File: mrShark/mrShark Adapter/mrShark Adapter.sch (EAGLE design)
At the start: 23 parts, among them CON1 DF12-20DS, IC1 LM317MBSTT3, IC2 MCP73832T-2DCI/OT, IC3 MCP73832T-2DCI/OT, IC4 FT232RQ

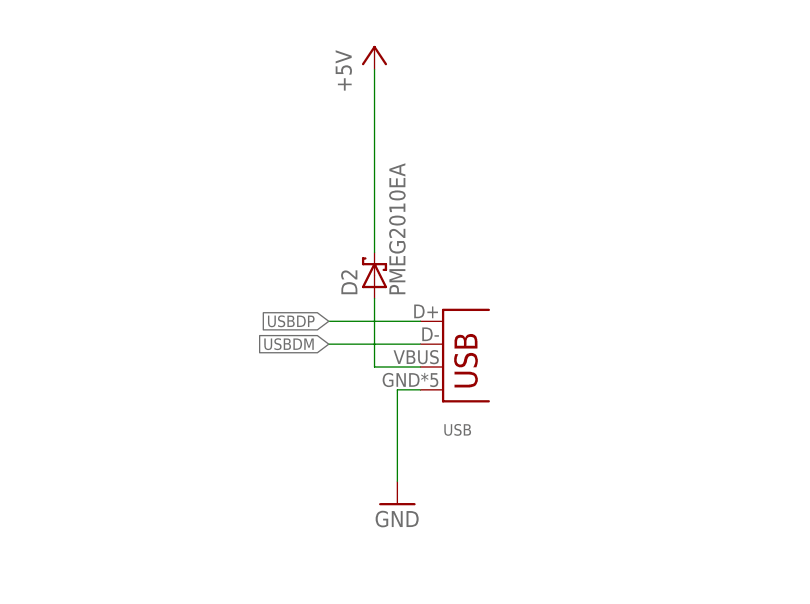
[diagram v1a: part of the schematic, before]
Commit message: Updated adapter to hirose mini usb connector
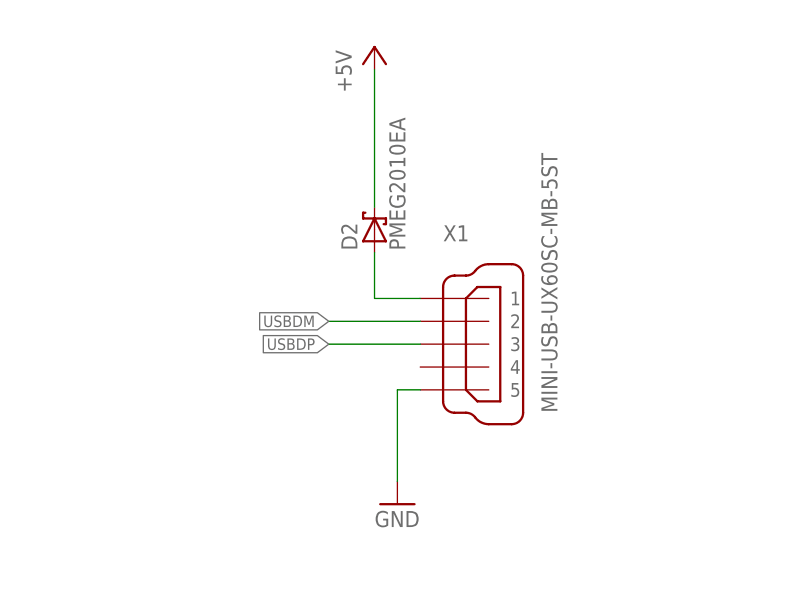
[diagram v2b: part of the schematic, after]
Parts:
- removed USB: (no value), con-usb-3:USB-MIC-S
- added X1: MINI-USB-UX60SC-MB-5ST, con-hirose:MINI-USB-UX60SC-MB-5ST
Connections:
- net GND: now also X1.5; no longer USB.GND
- net N$9: now also X1.1; no longer USB.VBUS
- net USBDM: now also X1.2; no longer USB.D-
- net USBDP: now also X1.3; no longer USB.D+
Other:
- moved on the sheet: D2
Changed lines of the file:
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@@
 <attribute name="TP_SIGNAL_NAME" value=""/>
 </part>
-<part name="USB" library="con-usb-3" deviceset="USB" device="-MIC-S"/>
 <part name="GND12" library="supply1" deviceset="GND" device=""/>
 <part name="D1" library="diode" deviceset="PMEG2010EA" device="R" value="PMEG2010EA"/>
@@
 <part name="P+4" library="supply1" deviceset="+5V" device=""/>
 <part name="P+10" library="supply1" deviceset="+5V" device=""/>
+<part name="X1" library="con-hirose" deviceset="MINI-USB-" device="UX60SC-MB-5ST"/>
 </parts>
 <sheets>
@@
 <instance part="TP4" gate="G$1" x="121.92" y="30.48"/>
 <instance part="TP5" gate="G$1" x="129.54" y="30.48"/>
-<instance part="USB" gate="G$1" x="127" y="129.54"/>
 <instance part="GND12" gate="1" x="121.92" y="116.84"/>
 <instance part="D1" gate="G$1" x="134.62" y="86.36" rot="R90"/>
-<instance part="D2" gate="G$1" x="119.38" y="142.24" rot="R90"/>
+<instance part="D2" gate="G$1" x="119.38" y="147.32" rot="R90"/>
 <instance part="ISP" gate="A" x="119.38" y="73.66"/>
 <instance part="P+4" gate="1" x="119.38" y="167.64"/>
 <instance part="P+10" gate="1" x="134.62" y="104.14"/>
+<instance part="X1" gate="G$1" x="129.54" y="134.62"/>
 </instances>
 <busses>
@@
 </segment>
 <segment>
-<pinref part="USB" gate="G$1" pin="GND"/>
 <pinref part="GND12" gate="1" pin="GND"/>
 <wire x1="124.46" y1="129.54" x2="121.92" y2="129.54" width="0.1524" layer="91"/>
 <wire x1="121.92" y1="129.54" x2="121.92" y2="119.38" width="0.1524" layer="91"/>
+<pinref part="X1" gate="G$1" pin="5"/>
 </segment>
 <segment>
@@
 <pinref part="D2" gate="G$1" pin="C"/>
 <pinref part="P+4" gate="1" pin="+5V"/>
-<wire x1="119.38" y1="144.78" x2="119.38" y2="165.1" width="0.1524" layer="91"/>
+<wire x1="119.38" y1="149.86" x2="119.38" y2="165.1" width="0.1524" layer="91"/>
 </segment>
 <segment>
@@
 </segment>
 <segment>
-<pinref part="USB" gate="G$1" pin="D+"/>
-<wire x1="124.46" y1="137.16" x2="114.3" y2="137.16" width="0.1524" layer="91"/>
-<label x="114.3" y="137.16" size="1.27" layer="95" rot="R180" xref="yes"/>
+<wire x1="124.46" y1="134.62" x2="114.3" y2="134.62" width="0.1524" layer="91"/>
+<label x="114.3" y="134.62" size="1.27" layer="95" rot="R180" xref="yes"/>
+<pinref part="X1" gate="G$1" pin="3"/>
 </segment>
 </net>
@@
 </segment>
 <segment>
-<pinref part="USB" gate="G$1" pin="D-"/>
-<wire x1="124.46" y1="134.62" x2="114.3" y2="134.62" width="0.1524" layer="91"/>
-<label x="114.3" y="134.62" size="1.27" layer="95" rot="R180" xref="yes"/>
+<wire x1="124.46" y1="137.16" x2="114.3" y2="137.16" width="0.1524" layer="91"/>
+<label x="114.3" y="137.16" size="1.27" layer="95" rot="R180" xref="yes"/>
+<pinref part="X1" gate="G$1" pin="2"/>
 </segment>
 </net>
 <net name="N$9" class="0">
 <segment>
-<pinref part="USB" gate="G$1" pin="VBUS"/>
-<wire x1="124.46" y1="132.08" x2="119.38" y2="132.08" width="0.1524" layer="91"/>
+<wire x1="124.46" y1="139.7" x2="119.38" y2="139.7" width="0.1524" layer="91"/>
 <pinref part="D2" gate="G$1" pin="A"/>
-<wire x1="119.38" y1="132.08" x2="119.38" y2="139.7" width="0.1524" layer="91"/>
-</segment>
-</net>
+<wire x1="119.38" y1="139.7" x2="119.38" y2="144.78" width="0.1524" layer="91"/>
+<pinref part="X1" gate="G$1" pin="1"/>
+</segment>
+</net>
